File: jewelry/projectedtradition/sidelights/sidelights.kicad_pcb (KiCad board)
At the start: 2 copper layers, 6 parts, among them J1 Conn_01x01, J2 Conn_01x01

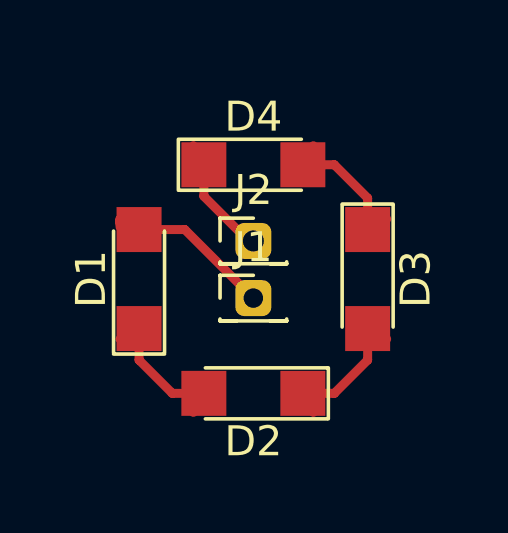
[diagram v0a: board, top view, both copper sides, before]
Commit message: jewelry: Complete initial LED driver layout
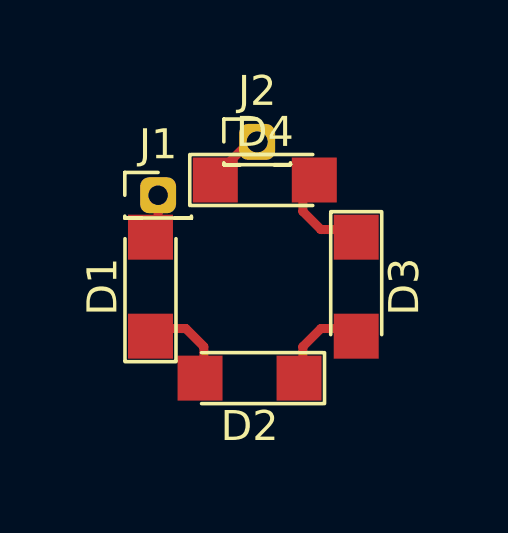
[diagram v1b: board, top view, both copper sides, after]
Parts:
- moved J1 4.67 mm to (45.7, 29.0)
- moved J2 3.30 mm to (49.0, 27.2)
- moved D4 0.63 mm to (49.3, 28.4)
- moved D2 0.52 mm to (48.8, 35.1)
- moved D1 0.46 mm to (45.5, 32.0)
- moved D3 0.46 mm to (52.3, 32.0)
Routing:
- net Net-(D1-Pad2): track 5.17 -> 1.50 mm
- net Net-(D2-Pad1): track 5.97 -> 3.08 mm
- net Net-(D3-Pad1): track 5.97 -> 3.08 mm
- net Net-(D1-Pad1): track 5.97 -> 3.08 mm
- net Net-(D4-Pad1): track 3.45 -> 1.69 mm
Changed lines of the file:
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@@
     (thickness 1.6)
     (drawings 3)
-    (tracks 23)
+    (tracks 16)
     (zones 0)
     (modules 6)
@@
     (47 F.CrtYd user)
     (48 B.Fab user)
-    (49 F.Fab user)
+    (49 F.Fab user hide)
   )
   (setup
@@
     (visible_elements FFFFFF7F)
     (pcbplotparams
-      (layerselection 0x010fc_ffffffff)
+      (layerselection 0x01000_ffffffff)
       (usegerberextensions false)
       (usegerberattributes false)
@@
       (padsonsilk false)
       (subtractmaskfromsilk false)
-      (outputformat 1)
+      (outputformat 3)
       (mirror false)
       (drillshape 1)
       (scaleselection 1)
-      (outputdirectory ""))
+      (outputdirectory ./out))
   )
   (net 0 "")
@@
   )
   (module Pin_Headers:Pin_Header_Straight_1x01_Pitch1.27mm (layer F.Cu)
-    (at 48.895 32.385)
+    (at 45.72 28.956)
     (descr "Through hole straight pin header, 1x01, 1.27mm pitch, single row")
     (tags "Through hole pin header THT 1x01 1.27mm single row")
@@
       (effects (font (size 1 1) (thickness 0.15)))
     )
-    (fp_text value Conn_01x01 (at 0 1.695) (layer F.Fab)
+    (fp_text value Conn_01x01 (at -7.874 0.254) (layer F.Fab)
       (effects (font (size 1 1) (thickness 0.15)))
     )
@@
   )
   (module Pin_Headers:Pin_Header_Straight_1x01_Pitch1.27mm (layer F.Cu)
-    (at 48.895 30.48)
+    (at 49.022 27.178)
     (descr "Through hole straight pin header, 1x01, 1.27mm pitch, single row")
     (tags "Through hole pin header THT 1x01 1.27mm single row")
@@
       (effects (font (size 1 1) (thickness 0.15)))
     )
-    (fp_text value Conn_01x01 (at 0 1.695) (layer F.Fab)
+    (fp_text value Conn_01x01 (at -7.874 0) (layer F.Fab)
       (effects (font (size 1 1) (thickness 0.15)))
     )
@@
   )
   (module LEDs:LED_1206 (layer F.Cu)
-    (at 45.085 31.75 90)
+    (at 45.466 32.004 90)
     (descr "LED 1206 smd package")
     (tags "LED led 1206 SMD smd SMT smt smdled SMDLED smtled SMTLED")
@@
   )
   (module LEDs:LED_1206 (layer F.Cu)
-    (at 48.895 35.56 180)
+    (at 48.768 35.052 180)
     (descr "LED 1206 smd package")
     (tags "LED led 1206 SMD smd SMT smt smdled SMDLED smtled SMTLED")
@@
   )
   (module LEDs:LED_1206 (layer F.Cu)
-    (at 52.705 31.75 270)
+    (at 52.324 32.004 270)
     (descr "LED 1206 smd package")
     (tags "LED led 1206 SMD smd SMT smt smdled SMDLED smtled SMTLED")
@@
   )
   (module LEDs:LED_1206 (layer F.Cu)
-    (at 48.895 27.94)
+    (at 49.276 28.448)
     (descr "LED 1206 smd package")
     (tags "LED led 1206 SMD smd SMT smt smdled SMDLED smtled SMTLED")
@@
     )
   )
-  (dimension 5.08 (width 0.3) (layer F.SilkS)
-    (gr_text "5.080 mm" (at 48.895 23.3) (layer F.SilkS)
+  (dimension 3.750265 (width 0.3) (layer F.SilkS)
+    (gr_text "3.750 mm" (at 45.160152 23.96114 28.30075577) (layer F.SilkS)
       (effects (font (size 1.5 1.5) (thickness 0.3)))
     )
-    (feature1 (pts (xy 51.435 26.67) (xy 51.435 24.813579)))
-    (feature2 (pts (xy 46.355 26.67) (xy 46.355 24.813579)))
-    (crossbar (pts (xy 46.355 25.4) (xy 51.435 25.4)))
-    (arrow1a (pts (xy 51.435 25.4) (xy 50.308496 25.986421)))
-    (arrow1b (pts (xy 51.435 25.4) (xy 50.308496 24.813579)))
-    (arrow2a (pts (xy 46.355 25.4) (xy 47.481504 25.986421)))
-    (arrow2b (pts (xy 46.355 25.4) (xy 47.481504 24.813579)))
+    (feature1 (pts (xy 49.022 27.178) (xy 47.52874 24.404802)))
+    (feature2 (pts (xy 45.72 28.956) (xy 44.22674 26.182802)))
+    (crossbar (pts (xy 44.504762 26.699129) (xy 47.806762 24.921129)))
+    (arrow1a (pts (xy 47.806762 24.921129) (xy 47.09293 25.971531)))
+    (arrow1b (pts (xy 47.806762 24.921129) (xy 46.536886 24.938878)))
+    (arrow2a (pts (xy 44.504762 26.699129) (xy 45.774638 26.68138)))
+    (arrow2b (pts (xy 44.504762 26.699129) (xy 45.218594 25.648727)))
   )
   (gr_circle (center 48.895 31.75) (end 59.895 31.75) (layer Eco1.User) (width 0.2))
   (gr_circle (center 48.895 31.75) (end 53.895 31.75) (layer Eco2.User) (width 0.2))
-  (segment (start 46.895 35.045) (end 46.895 36.195) (width 0.3) (layer F.Cu) (net 1))
-  (segment (start 44.45 33.75) (end 45.6 33.75) (width 0.3) (layer F.Cu) (net 1))
-  (segment (start 46.195 35.56) (end 47.245 35.56) (width 0.3) (layer F.Cu) (net 1))
-  (segment (start 45.085 34.45) (end 46.195 35.56) (width 0.3) (layer F.Cu) (net 1))
-  (segment (start 45.085 33.4) (end 45.085 34.45) (width 0.3) (layer F.Cu) (net 1))
-  (segment (start 44.45 30.01) (end 44.45 29.75) (width 0.3) (layer F.Cu) (net 2))
-  (segment (start 44.45 29.9) (end 44.45 29.75) (width 0.3) (layer F.Cu) (net 2))
-  (segment (start 46.61 30.1) (end 48.895 32.385) (width 0.3) (layer F.Cu) (net 2))
-  (segment (start 45.085 30.1) (end 46.61 30.1) (width 0.3) (layer F.Cu) (net 2))
-  (segment (start 52.19 33.75) (end 53.34 33.75) (width 0.3) (layer F.Cu) (net 3))
-  (segment (start 50.895 36.195) (end 50.895 35.045) (width 0.3) (layer F.Cu) (net 3))
-  (segment (start 52.705 34.45) (end 52.705 33.4) (width 0.3) (layer F.Cu) (net 3))
-  (segment (start 51.595 35.56) (end 52.705 34.45) (width 0.3) (layer F.Cu) (net 3))
-  (segment (start 50.545 35.56) (end 51.595 35.56) (width 0.3) (layer F.Cu) (net 3))
-  (segment (start 50.895 28.455) (end 50.895 27.305) (width 0.3) (layer F.Cu) (net 4))
-  (segment (start 53.34 29.75) (end 52.19 29.75) (width 0.3) (layer F.Cu) (net 4))
-  (segment (start 51.595 27.94) (end 50.545 27.94) (width 0.3) (layer F.Cu) (net 4))
-  (segment (start 52.705 29.05) (end 51.595 27.94) (width 0.3) (layer F.Cu) (net 4))
-  (segment (start 52.705 30.1) (end 52.705 29.05) (width 0.3) (layer F.Cu) (net 4))
-  (segment (start 46.99 27.4) (end 46.895 27.305) (width 0.3) (layer F.Cu) (net 5))
-  (segment (start 48.735 30.48) (end 48.895 30.48) (width 0.3) (layer F.Cu) (net 5))
-  (segment (start 47.245 28.99) (end 48.735 30.48) (width 0.3) (layer F.Cu) (net 5))
-  (segment (start 47.245 27.94) (end 47.245 28.99) (width 0.3) (layer F.Cu) (net 5))
+  (segment (start 46.516 33.4) (end 45.466 33.4) (width 0.3) (layer F.Cu) (net 1))
+  (segment (start 46.643 33.4) (end 46.516 33.4) (width 0.3) (layer F.Cu) (net 1))
+  (segment (start 47.245 34.002) (end 46.643 33.4) (width 0.3) (layer F.Cu) (net 1))
+  (segment (start 47.245 35.052) (end 47.245 34.002) (width 0.3) (layer F.Cu) (net 1))
+  (segment (start 45.72 30.1) (end 45.466 30.354) (width 0.3) (layer F.Cu) (net 2))
+  (segment (start 45.72 28.956) (end 45.72 30.1) (width 0.3) (layer F.Cu) (net 2))
+  (segment (start 51.274 33.4) (end 52.324 33.4) (width 0.3) (layer F.Cu) (net 3))
+  (segment (start 51.147 33.4) (end 51.274 33.4) (width 0.3) (layer F.Cu) (net 3))
+  (segment (start 50.545 34.002) (end 51.147 33.4) (width 0.3) (layer F.Cu) (net 3))
+  (segment (start 50.545 35.052) (end 50.545 34.002) (width 0.3) (layer F.Cu) (net 3))
+  (segment (start 51.274 30.1) (end 52.324 30.1) (width 0.3) (layer F.Cu) (net 4))
+  (segment (start 51.147 30.1) (end 51.274 30.1) (width 0.3) (layer F.Cu) (net 4))
+  (segment (start 50.545 29.498) (end 51.147 30.1) (width 0.3) (layer F.Cu) (net 4))
+  (segment (start 50.545 28.448) (end 50.545 29.498) (width 0.3) (layer F.Cu) (net 4))
+  (segment (start 47.498 28.448) (end 48.514 27.432) (width 0.3) (layer F.Cu) (net 5))
+  (segment (start 47.245 28.448) (end 47.498 28.448) (width 0.3) (layer F.Cu) (net 5))
 )

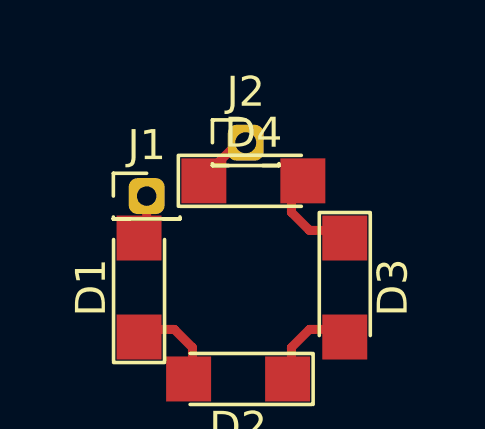
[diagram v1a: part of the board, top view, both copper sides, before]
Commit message: jewelry: New PCB ready for test
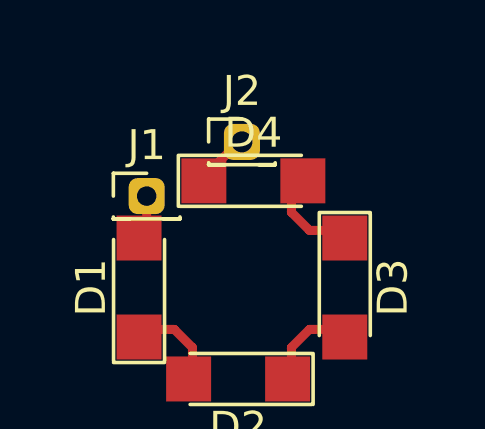
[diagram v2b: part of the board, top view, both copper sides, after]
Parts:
- moved J2 0.13 mm to (48.9, 27.1)
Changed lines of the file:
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@@
   (general
     (thickness 1.6)
-    (drawings 3)
+    (drawings 2)
     (tracks 16)
     (zones 0)
@@
   )
   (module Pin_Headers:Pin_Header_Straight_1x01_Pitch1.27mm (layer F.Cu)
-    (at 49.022 27.178)
+    (at 48.895 27.15)
     (descr "Through hole straight pin header, 1x01, 1.27mm pitch, single row")
     (tags "Through hole pin header THT 1x01 1.27mm single row")
@@
     )
   )
-  (dimension 3.750265 (width 0.3) (layer F.SilkS)
-    (gr_text "3.750 mm" (at 45.160152 23.96114 28.30075577) (layer F.SilkS)
-      (effects (font (size 1.5 1.5) (thickness 0.3)))
-    )
-    (feature1 (pts (xy 49.022 27.178) (xy 47.52874 24.404802)))
-    (feature2 (pts (xy 45.72 28.956) (xy 44.22674 26.182802)))
-    (crossbar (pts (xy 44.504762 26.699129) (xy 47.806762 24.921129)))
-    (arrow1a (pts (xy 47.806762 24.921129) (xy 47.09293 25.971531)))
-    (arrow1b (pts (xy 47.806762 24.921129) (xy 46.536886 24.938878)))
-    (arrow2a (pts (xy 44.504762 26.699129) (xy 45.774638 26.68138)))
-    (arrow2b (pts (xy 44.504762 26.699129) (xy 45.218594 25.648727)))
-  )
+  (gr_circle (center 48.895 31.75) (end 53.895 31.75) (layer Eco2.User) (width 0.2))
   (gr_circle (center 48.895 31.75) (end 59.895 31.75) (layer Eco1.User) (width 0.2))
-  (gr_circle (center 48.895 31.75) (end 53.895 31.75) (layer Eco2.User) (width 0.2))
   (segment (start 46.516 33.4) (end 45.466 33.4) (width 0.3) (layer F.Cu) (net 1))
   (segment (start 46.643 33.4) (end 46.516 33.4) (width 0.3) (layer F.Cu) (net 1))

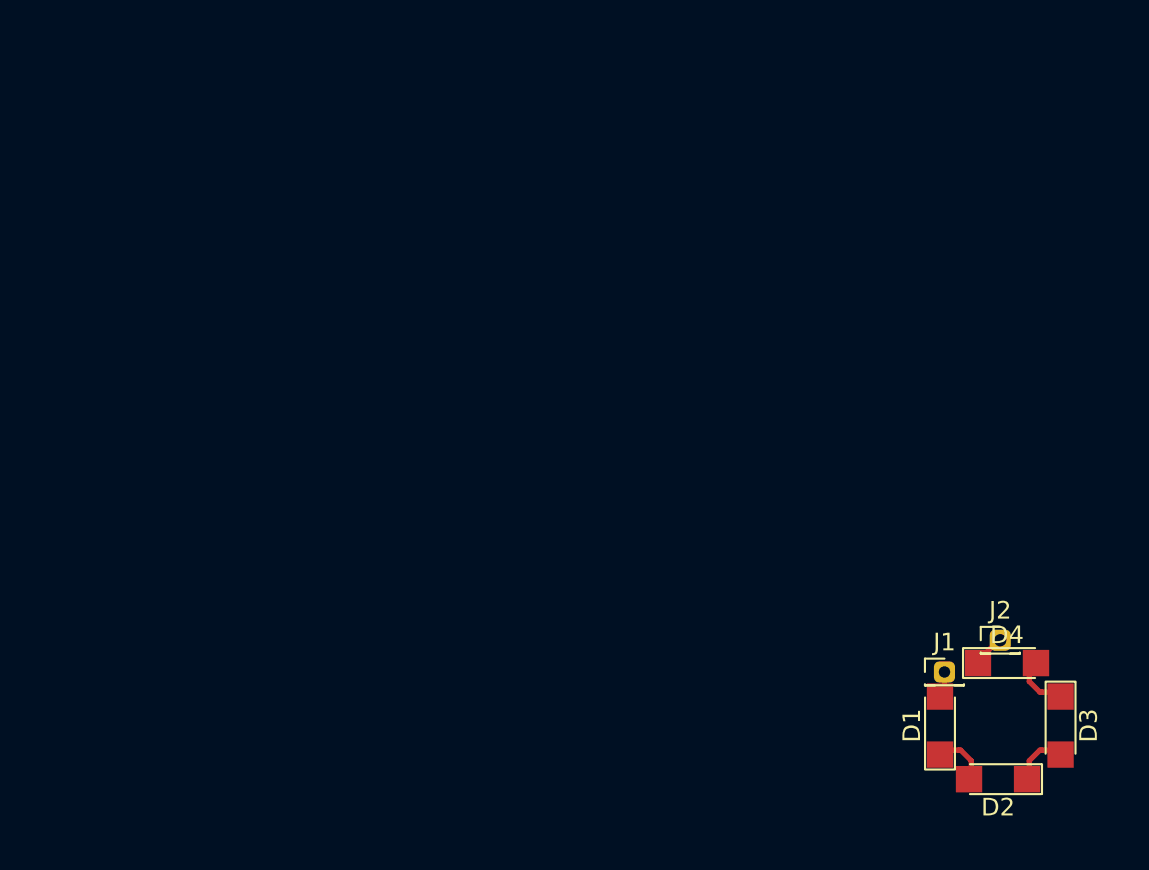
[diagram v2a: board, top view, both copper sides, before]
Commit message: jewerly: Milled PCB
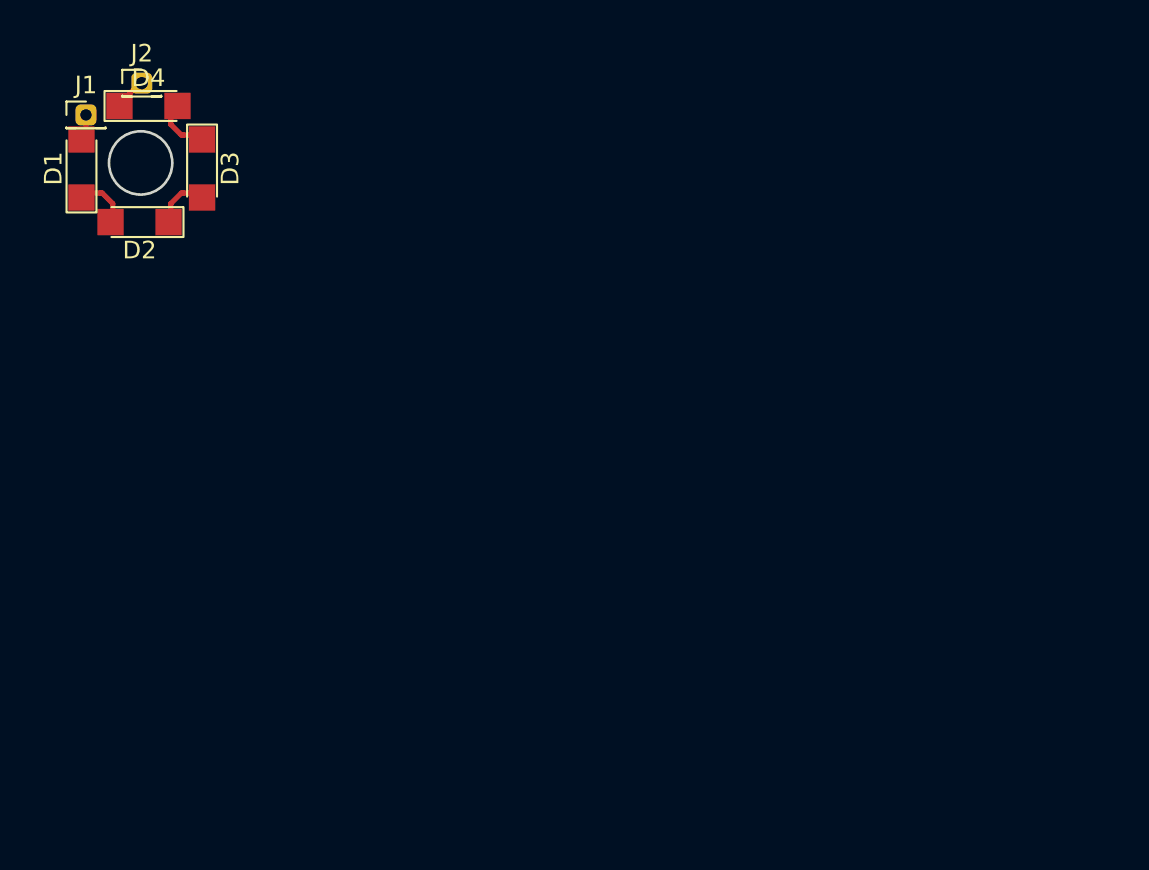
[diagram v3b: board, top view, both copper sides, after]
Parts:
- moved D4 58.2 mm to (0.44, -3.24)
- moved J2 58.2 mm to (0.06, -4.54)
- moved D1 58.2 mm to (-3.37, 0.32)
- moved D2 58.2 mm to (-0.06, 3.37)
- moved D3 58.2 mm to (3.49, 0.32)
- moved J1 58.2 mm to (-3.11, -2.73)
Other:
- board outline added: 3.6 x 3.6 mm
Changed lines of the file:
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@@
   (general
     (thickness 1.6)
-    (drawings 2)
+    (drawings 3)
     (tracks 16)
     (zones 0)
@@
     (visible_elements FFFFFF7F)
     (pcbplotparams
-      (layerselection 0x01000_ffffffff)
+      (layerselection 0x01000_7fffffff)
       (usegerberextensions false)
       (usegerberattributes false)
@@
       (padsonsilk false)
       (subtractmaskfromsilk false)
-      (outputformat 3)
+      (outputformat 5)
       (mirror false)
       (drillshape 1)
@@
   )
   (module Pin_Headers:Pin_Header_Straight_1x01_Pitch1.27mm (layer F.Cu)
-    (at 45.72 28.956)
+    (at -3.1115 -2.7305)
     (descr "Through hole straight pin header, 1x01, 1.27mm pitch, single row")
     (tags "Through hole pin header THT 1x01 1.27mm single row")
@@
   )
   (module Pin_Headers:Pin_Header_Straight_1x01_Pitch1.27mm (layer F.Cu)
-    (at 48.895 27.15)
+    (at 0.0635 -4.5365)
     (descr "Through hole straight pin header, 1x01, 1.27mm pitch, single row")
     (tags "Through hole pin header THT 1x01 1.27mm single row")
@@
   )
   (module LEDs:LED_1206 (layer F.Cu)
-    (at 45.466 32.004 90)
+    (at -3.3655 0.3175 90)
     (descr "LED 1206 smd package")
     (tags "LED led 1206 SMD smd SMT smt smdled SMDLED smtled SMTLED")
@@
   )
   (module LEDs:LED_1206 (layer F.Cu)
-    (at 48.768 35.052 180)
+    (at -0.0635 3.3655 180)
     (descr "LED 1206 smd package")
     (tags "LED led 1206 SMD smd SMT smt smdled SMDLED smtled SMTLED")
@@
   )
   (module LEDs:LED_1206 (layer F.Cu)
-    (at 52.324 32.004 270)
+    (at 3.4925 0.3175 270)
     (descr "LED 1206 smd package")
     (tags "LED led 1206 SMD smd SMT smt smdled SMDLED smtled SMTLED")
@@
   )
   (module LEDs:LED_1206 (layer F.Cu)
-    (at 49.276 28.448)
+    (at 0.4445 -3.2385)
     (descr "LED 1206 smd package")
     (tags "LED led 1206 SMD smd SMT smt smdled SMDLED smtled SMTLED")
@@
     )
   )
-  (gr_circle (center 48.895 31.75) (end 53.895 31.75) (layer Eco2.User) (width 0.2))
-  (gr_circle (center 48.895 31.75) (end 59.895 31.75) (layer Eco1.User) (width 0.2))
-  (segment (start 46.516 33.4) (end 45.466 33.4) (width 0.3) (layer F.Cu) (net 1))
-  (segment (start 46.643 33.4) (end 46.516 33.4) (width 0.3) (layer F.Cu) (net 1))
-  (segment (start 47.245 34.002) (end 46.643 33.4) (width 0.3) (layer F.Cu) (net 1))
-  (segment (start 47.245 35.052) (end 47.245 34.002) (width 0.3) (layer F.Cu) (net 1))
-  (segment (start 45.72 30.1) (end 45.466 30.354) (width 0.3) (layer F.Cu) (net 2))
-  (segment (start 45.72 28.956) (end 45.72 30.1) (width 0.3) (layer F.Cu) (net 2))
-  (segment (start 51.274 33.4) (end 52.324 33.4) (width 0.3) (layer F.Cu) (net 3))
-  (segment (start 51.147 33.4) (end 51.274 33.4) (width 0.3) (layer F.Cu) (net 3))
-  (segment (start 50.545 34.002) (end 51.147 33.4) (width 0.3) (layer F.Cu) (net 3))
-  (segment (start 50.545 35.052) (end 50.545 34.002) (width 0.3) (layer F.Cu) (net 3))
-  (segment (start 51.274 30.1) (end 52.324 30.1) (width 0.3) (layer F.Cu) (net 4))
-  (segment (start 51.147 30.1) (end 51.274 30.1) (width 0.3) (layer F.Cu) (net 4))
-  (segment (start 50.545 29.498) (end 51.147 30.1) (width 0.3) (layer F.Cu) (net 4))
-  (segment (start 50.545 28.448) (end 50.545 29.498) (width 0.3) (layer F.Cu) (net 4))
-  (segment (start 47.498 28.448) (end 48.514 27.432) (width 0.3) (layer F.Cu) (net 5))
-  (segment (start 47.245 28.448) (end 47.498 28.448) (width 0.3) (layer F.Cu) (net 5))
+  (gr_circle (center 0 0) (end 1.8 0) (layer Edge.Cuts) (width 0.15))
+  (gr_circle (center 0 0) (end 5 0) (layer Eco2.User) (width 0.2))
+  (gr_circle (center 0 0) (end 11 0) (layer Eco1.User) (width 0.2))
+  (segment (start -2.3155 1.7135) (end -3.3655 1.7135) (width 0.3) (layer F.Cu) (net 1))
+  (segment (start -2.1885 1.7135) (end -2.3155 1.7135) (width 0.3) (layer F.Cu) (net 1))
+  (segment (start -1.5865 2.3155) (end -2.1885 1.7135) (width 0.3) (layer F.Cu) (net 1))
+  (segment (start -1.5865 3.3655) (end -1.5865 2.3155) (width 0.3) (layer F.Cu) (net 1))
+  (segment (start -3.1115 -1.5865) (end -3.3655 -1.3325) (width 0.3) (layer F.Cu) (net 2))
+  (segment (start -3.1115 -2.7305) (end -3.1115 -1.5865) (width 0.3) (layer F.Cu) (net 2))
+  (segment (start 2.4425 1.7135) (end 3.4925 1.7135) (width 0.3) (layer F.Cu) (net 3))
+  (segment (start 2.3155 1.7135) (end 2.4425 1.7135) (width 0.3) (layer F.Cu) (net 3))
+  (segment (start 1.7135 2.3155) (end 2.3155 1.7135) (width 0.3) (layer F.Cu) (net 3))
+  (segment (start 1.7135 3.3655) (end 1.7135 2.3155) (width 0.3) (layer F.Cu) (net 3))
+  (segment (start 2.4425 -1.5865) (end 3.4925 -1.5865) (width 0.3) (layer F.Cu) (net 4))
+  (segment (start 2.3155 -1.5865) (end 2.4425 -1.5865) (width 0.3) (layer F.Cu) (net 4))
+  (segment (start 1.7135 -2.1885) (end 2.3155 -1.5865) (width 0.3) (layer F.Cu) (net 4))
+  (segment (start 1.7135 -3.2385) (end 1.7135 -2.1885) (width 0.3) (layer F.Cu) (net 4))
+  (segment (start -1.3335 -3.2385) (end -0.3175 -4.2545) (width 0.3) (layer F.Cu) (net 5))
+  (segment (start -1.5865 -3.2385) (end -1.3335 -3.2385) (width 0.3) (layer F.Cu) (net 5))
 )
